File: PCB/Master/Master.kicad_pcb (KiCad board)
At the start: 2 copper layers, 67.7 x 40.1 mm, 63 parts, among them J1 USB_C_Receptacle_USB2.0_16P, J2 Conn_01x05_Pin, J5 Conn_01x09_Pin, J6 Conn_01x09_Pin, Q2 AO3400A, Q3 AO3400A, SW1 PTS810_SJM_250_SMTR_LFS, SW2 PTS810_SJM_250_SMTR_LFS, U1 ESP32-S3-WROOM-1U, U2 TCA9406DC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

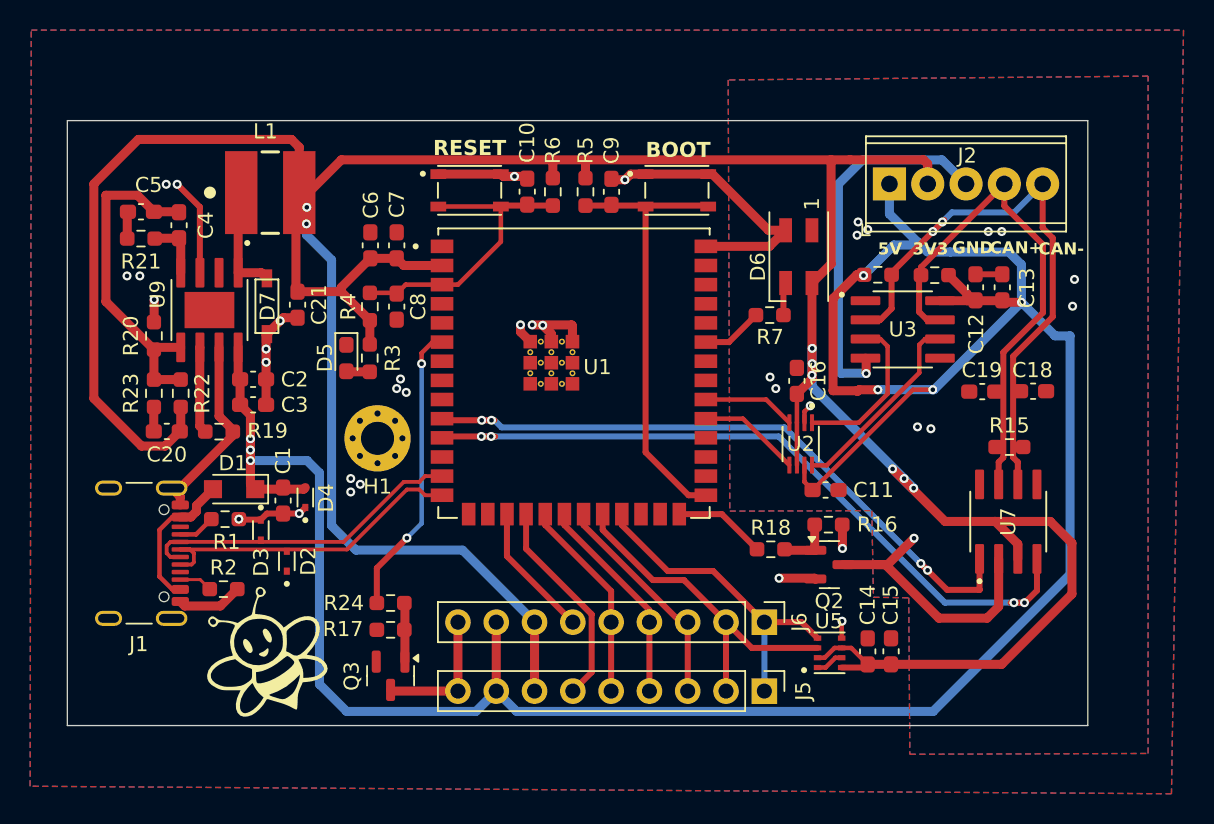
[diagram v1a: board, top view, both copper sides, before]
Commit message: Small changes to the pcb(Master and Slave))
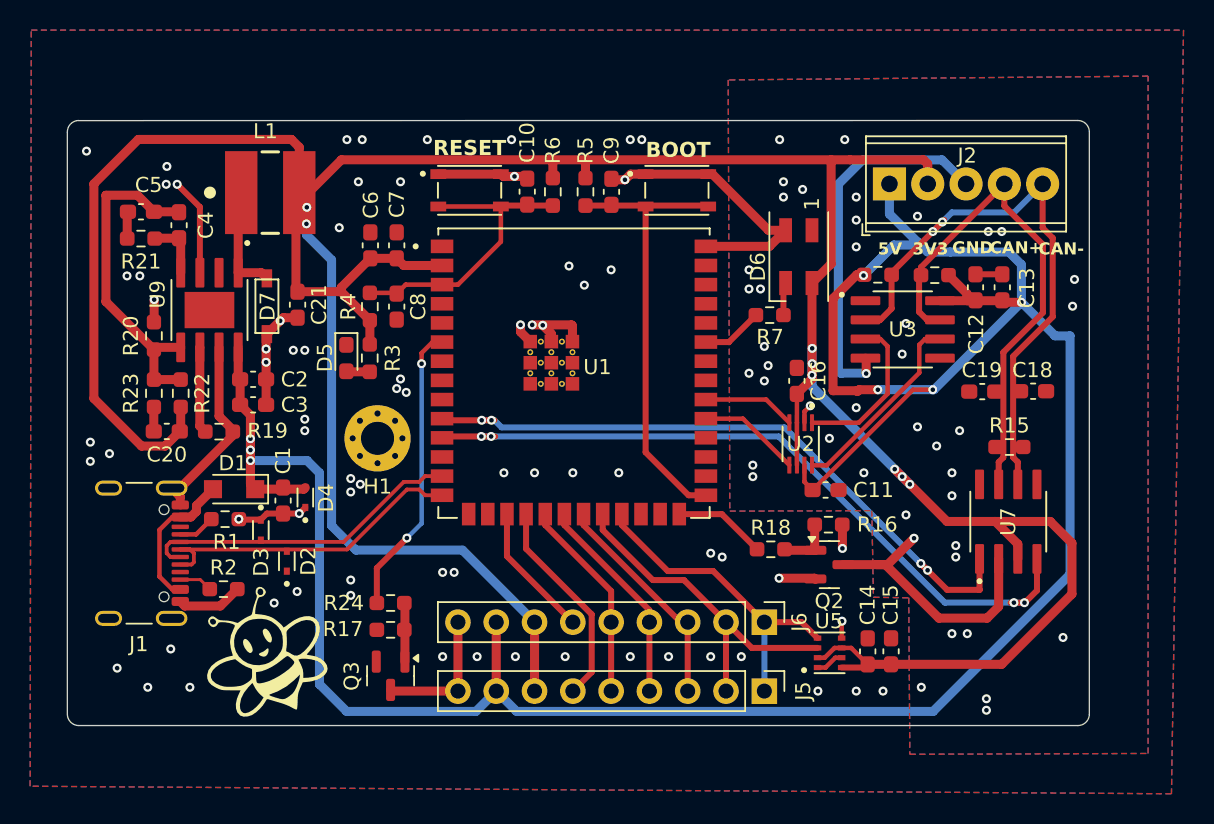
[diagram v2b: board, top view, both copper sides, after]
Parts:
- C10, C13, C7, C9: value 0u1F -> 100nF
- C11, C16: value u1F -> 100nF
- C14: value 0u1F -> 100nf
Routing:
- net ESP_3V3: track 232.7 -> 230.2 mm
- net GND_OUT: vias 14 -> 44
- net GND: vias 24 -> 72
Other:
- board size 67.7 x 40.1 mm -> 67.8 x 40.1 mm

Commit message: Added CAP
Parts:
- added C17: 100nf, Capacitor_SMD:C_0603_1608Metric_Pad1.08x0.95mm_HandSolder, F.Cu at (92.2, 55.4)
- added C22: 1uF, Capacitor_SMD:C_0603_1608Metric_Pad1.08x0.95mm_HandSolder, F.Cu at (93.8, 55.4)
- added C23: 1uf, Capacitor_SMD:C_0603_1608Metric_Pad1.08x0.95mm_HandSolder, F.Cu at (82.0, 52.6)
- added C24: 1uf, Capacitor_SMD:C_0603_1608Metric_Pad1.08x0.95mm_HandSolder, F.Cu at (81.8, 45.3)
- moved C11 0.13 mm to (85.4, 52.6)
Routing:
- net GND_OUT: track 47.0 -> 61.5 mm
- net VCC_5V: track 176.9 -> 178.6 mm
- net ESP_3V3: track 230.2 -> 231.9 mm

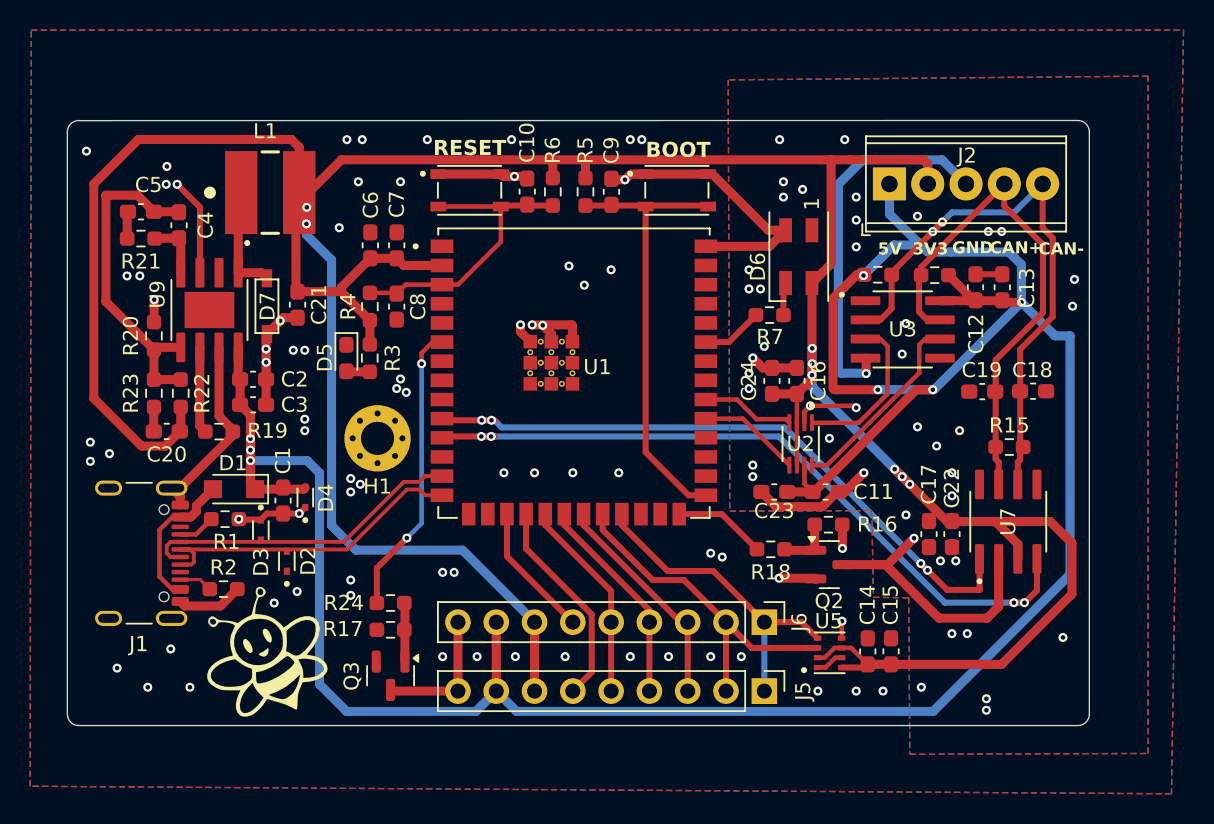
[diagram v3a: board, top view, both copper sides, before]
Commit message: From 0603 TO 0805 at power supply
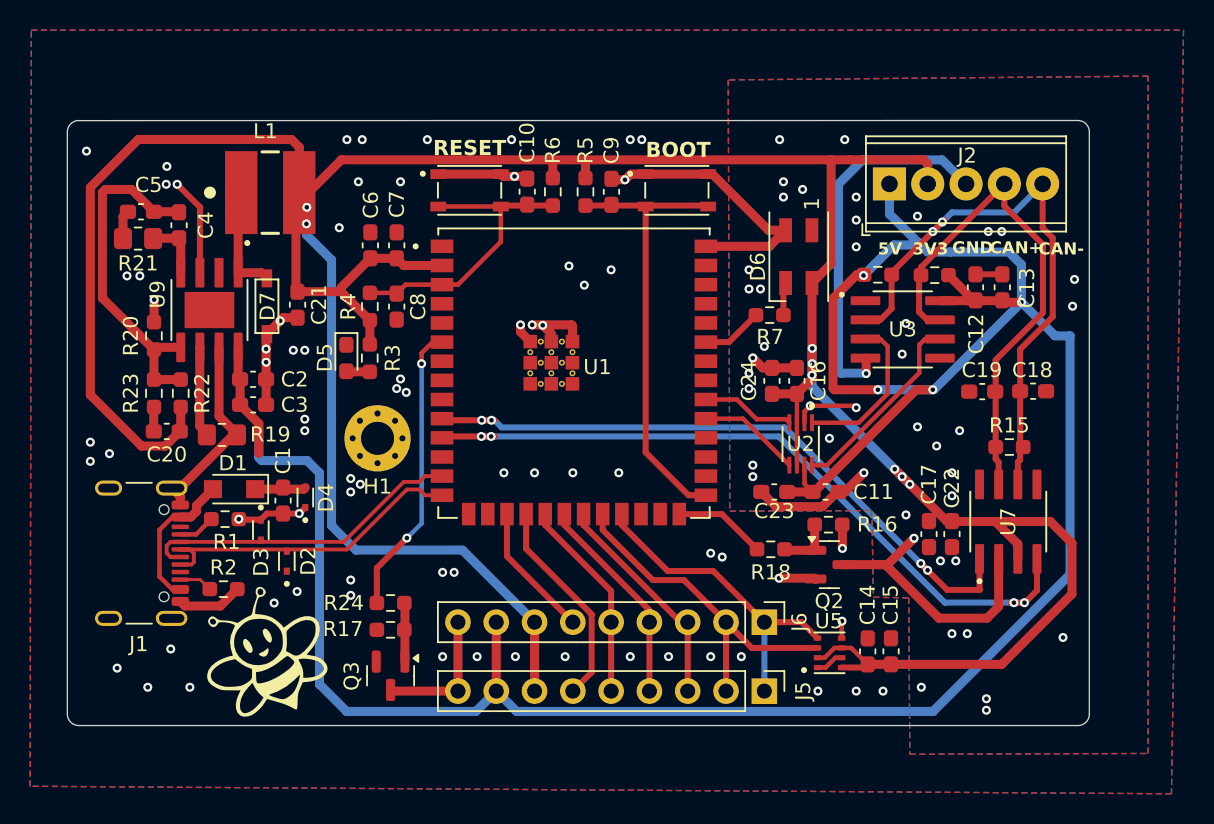
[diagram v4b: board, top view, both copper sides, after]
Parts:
- R19, R21: footprint Resistor_SMD:R_0603_1608Metric_Pad0.98x0.95mm_HandSolder -> Resistor_SMD:R_0805_2012Metric_Pad1.20x1.40mm_HandSolder
- moved R19 0.29 mm to (45.3, 48.8)
- moved R21 0.19 mm to (39.8, 35.8)
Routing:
- net VCC_5V: track 178.6 -> 176.9 mm, vias 7 -> 4
- net Net-(U9-FB): track 22.5 -> 23.2 mm

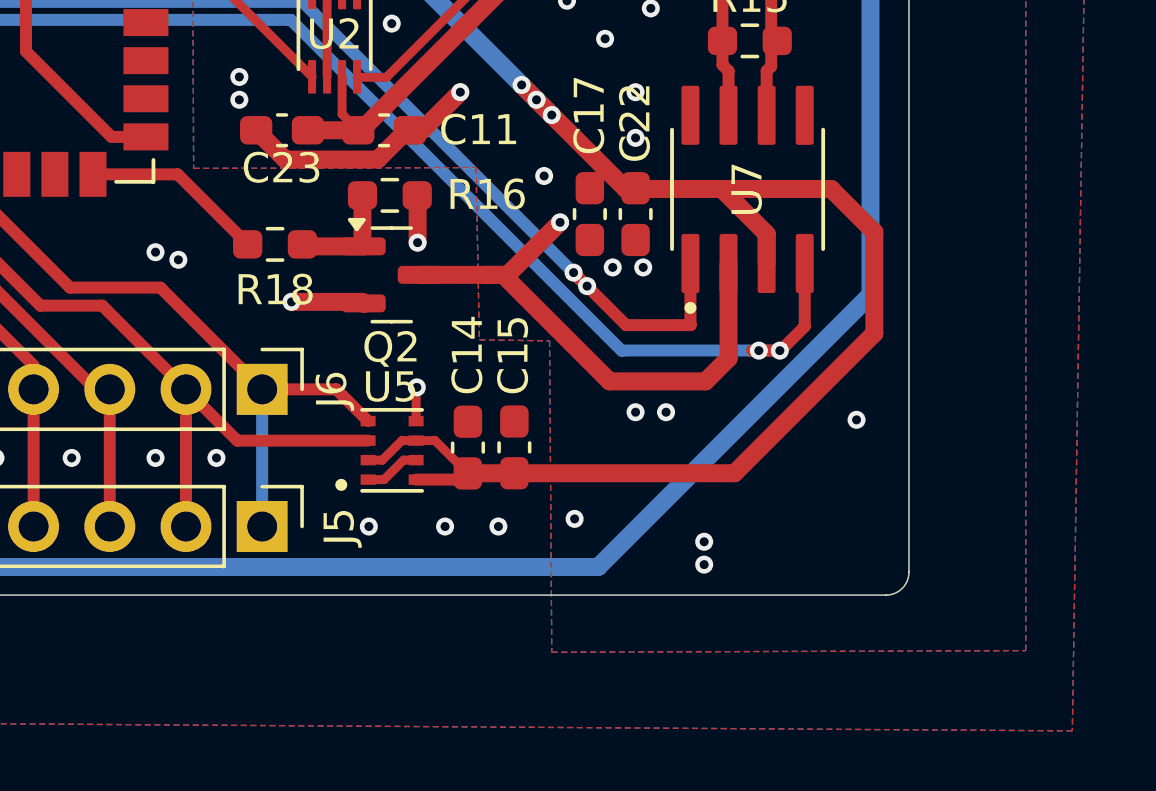
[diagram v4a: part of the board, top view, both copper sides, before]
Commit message: Changed bmp for bme
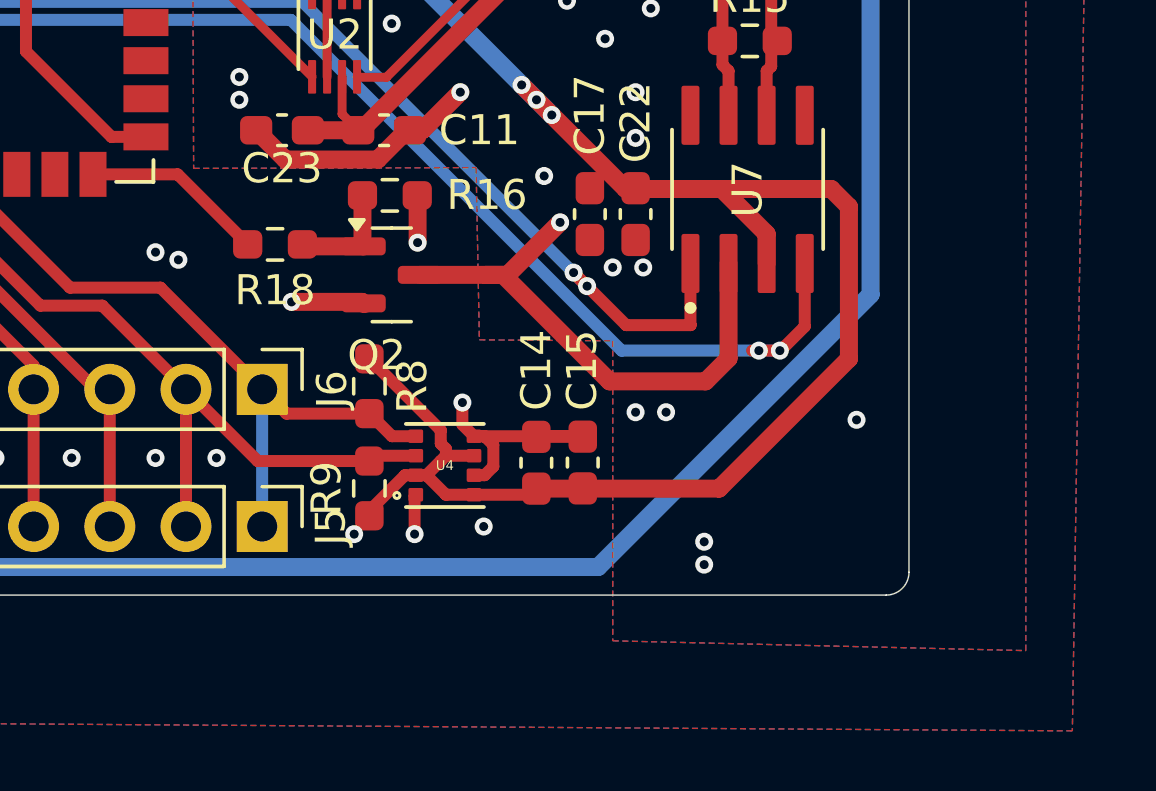
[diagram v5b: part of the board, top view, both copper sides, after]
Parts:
- removed U5: BMP280, BMP280:XDCR_BMP280
- added R8: 4k7, Resistor_SMD:R_0603_1608Metric_Pad0.98x0.95mm_HandSolder, F.Cu at (84.9, 61.2)
- added R9: 4k7, Resistor_SMD:R_0603_1608Metric_Pad0.98x0.95mm_HandSolder, F.Cu at (84.9, 64.6)
- added U4: BME280, BME280:PSON65P250X250X100-8N, F.Cu at (87.4, 63.8)
- R22: value 45k -> 47k
- moved C14 2.34 mm to (90.5, 63.7)
- moved C15 2.34 mm to (92.0, 63.7)
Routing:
- net GND: track 75.9 -> 82.9 mm
- net ESP_3V3: track 232.1 -> 236.5 mm
- net I2C_SDA: track 23.1 -> 25.1 mm
- net I2C_SCK: track 21.4 -> 23.2 mm
- net GND_OUT: vias 44 -> 43

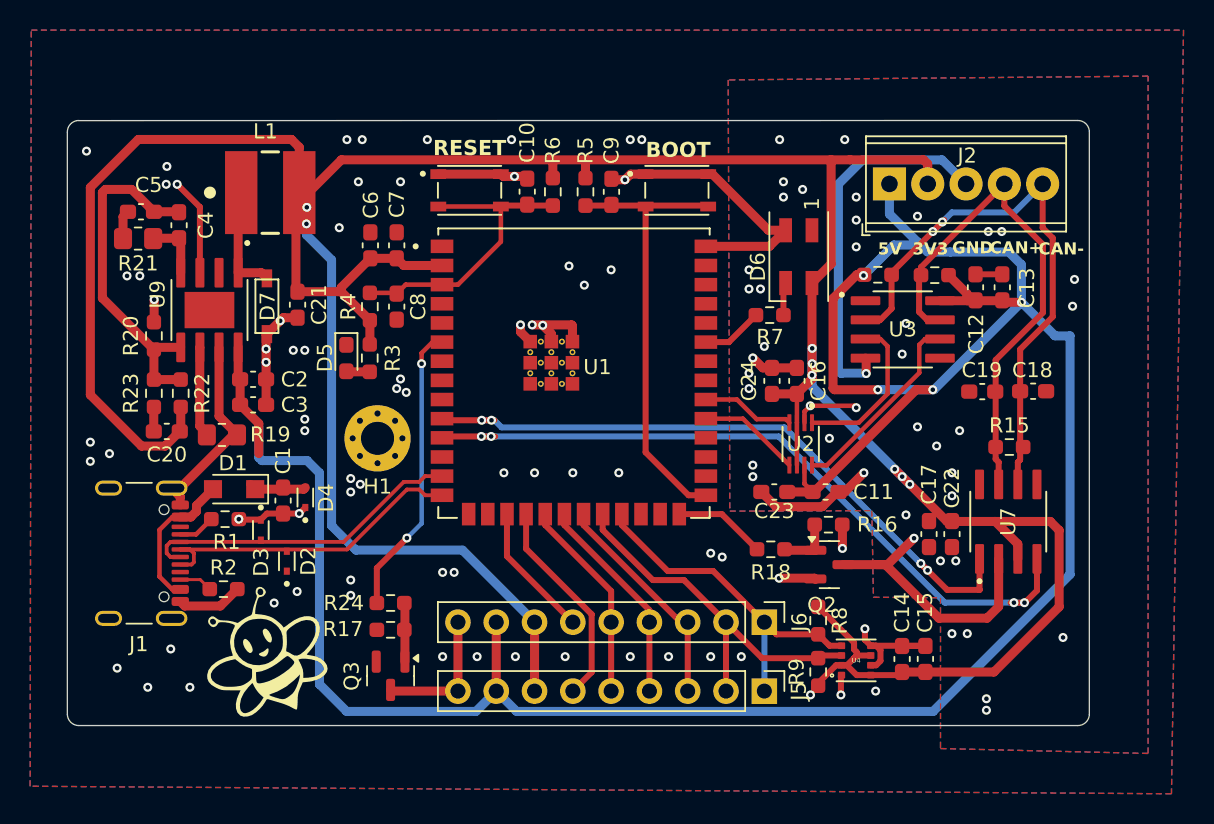
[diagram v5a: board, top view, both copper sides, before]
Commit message: Added I2C PullUp Resistors
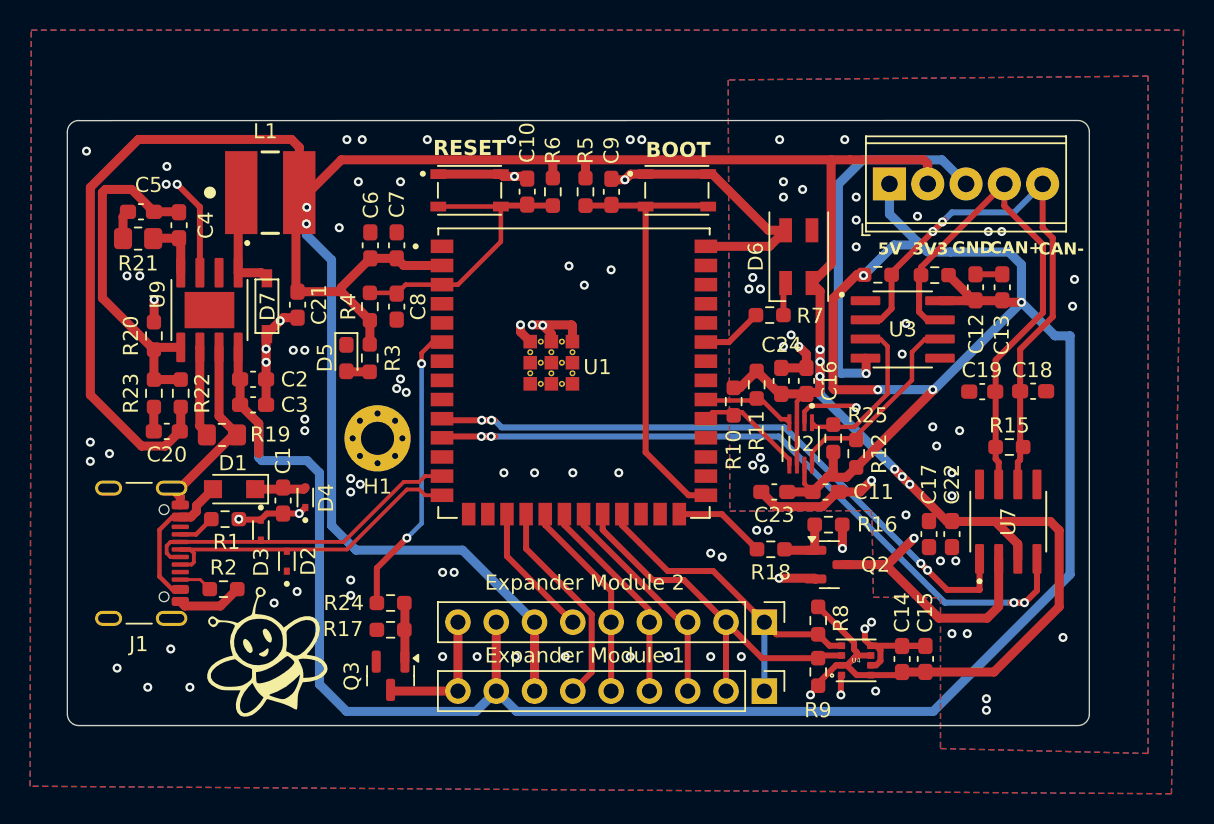
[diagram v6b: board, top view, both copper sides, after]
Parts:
- added R10: 4k7, Resistor_SMD:R_0603_1608Metric_Pad0.98x0.95mm_HandSolder, F.Cu at (79.3, 46.6)
- added R11: 4k7, Resistor_SMD:R_0603_1608Metric_Pad0.98x0.95mm_HandSolder, F.Cu at (80.8, 45.5)
- added R12: 4k7, Resistor_SMD:R_0603_1608Metric_Pad0.98x0.95mm_HandSolder, F.Cu at (87.4, 50.1)
- added R25: 4k7, Resistor_SMD:R_0603_1608Metric_Pad0.98x0.95mm_HandSolder, F.Cu at (85.9, 49.1)
- moved C16 0.64 mm to (84.1, 45.3)
- moved C24 0.61 mm to (82.4, 45.3)
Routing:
- net ESP_3V3: track 236.5 -> 241.2 mm
- net VCC_5V: track 176.9 -> 178.8 mm
- net SCL_ESP: track 6.81 -> 7.38 mm
- net GND_OUT: track 61.5 -> 62.0 mm, vias 43 -> 41
- net GND: vias 72 -> 75
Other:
- board text added: "Expander Module 1"
- board text added: "Expander Module 2"

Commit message: repaired HX711
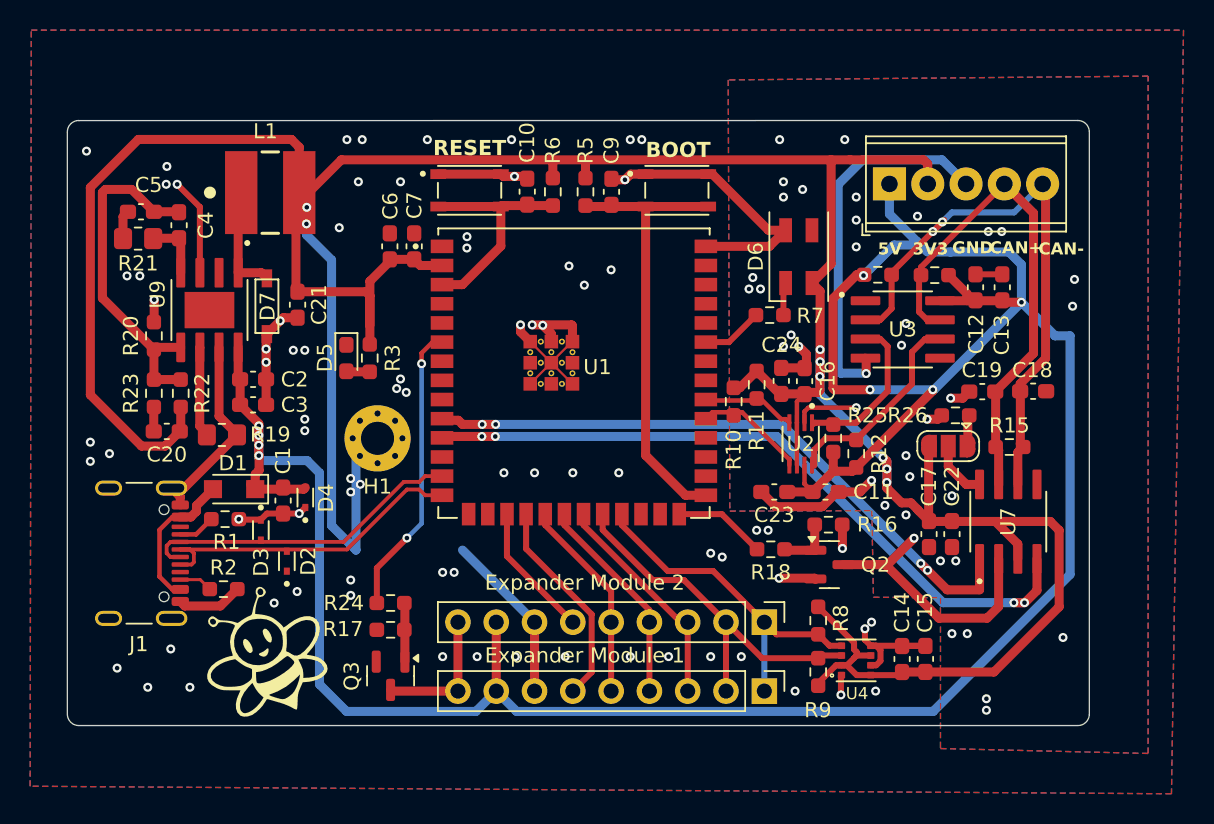
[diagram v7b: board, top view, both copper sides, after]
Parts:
- removed C8: 1uf, Capacitor_SMD:C_0603_1608Metric_Pad1.08x0.95mm_HandSolder
- removed R4: 10k, Resistor_SMD:R_0603_1608Metric_Pad0.98x0.95mm_HandSolder
- added JP1: SolderJumper_3_Open, Jumper:SolderJumper-3_P1.3mm_Open_RoundedPad1.0x1.5mm, F.Cu at (93.5, 49.6)
- added R26: R, Resistor_SMD:R_0603_1608Metric_Pad0.98x0.95mm_HandSolder, F.Cu at (94.0, 47.5)
- moved C6 1.29 mm to (56.5, 36.3)
- moved C7 1.16 mm to (58.1, 36.3)
- moved C16 0.13 mm to (84.0, 45.3)
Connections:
- U7 pad 8: unconnected-(U7-RS-Pad8) -> CAN_RS
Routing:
- net GND: track 82.9 -> 91.0 mm, vias 75 -> 77
- net ESP_3V3: track 241.2 -> 249.1 mm
- net CHIP_PU: track 20.4 -> 15.5 mm
- net CAN_RS: track 0.00 -> 3.92 mm
- net GND_OUT: track 62.0 -> 64.5 mm, vias 41 -> 39
- net Net-(JP1-A): track 0.00 -> 2.23 mm
- net VCC_5V: track 178.8 -> 180.7 mm, vias 4 -> 8
- net TX_CAN: track 44.9 -> 45.5 mm

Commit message: V3
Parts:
- added G***: LOGO, LOGO, B.Cu at (41.1, 33.4)
- moved G*** 0.26 mm to (48.1, 63.1)
- moved R2 0.16 mm to (45.3, 59.1)
- moved C1 0.16 mm to (49.2, 53.2)
- moved D1 0.16 mm to (46.0, 52.4)
- moved D2 0.16 mm to (49.5, 57.2)
- moved D3 0.16 mm to (47.8, 55.2)
- moved D4 0.16 mm to (50.7, 53.0)
- moved J1 0.16 mm to (38.7, 56.7)
- moved R1 0.16 mm to (45.4, 54.4)
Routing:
- net GND: track 91.0 -> 92.9 mm, vias 77 -> 78
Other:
- board size 67.8 x 40.1 mm -> 68 x 40 mm
- board text added: "SMART HIVE MASTER V3"
